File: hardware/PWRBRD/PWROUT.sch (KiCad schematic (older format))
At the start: 0 parts

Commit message: Should now ACTUALLY include power distribution schematic.
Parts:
- added C? (x2): 10uF, symbol C
- added C? (x3): 22uF, symbol C
- added C?: 50nF, symbol C
- added D?: D_Schottky, symbol D_Schottky
- added L?: 1uH, symbol INDUCTOR
- added L?: 4.7uF, symbol INDUCTOR
- added L?: 4mH, symbol INDUCTOR
- added Q?: Q_NPN_BCE, symbol Q_NPN_BCE
- added R?: 10k, symbol R
- added R?: 100m, symbol R
- added R?: 51K, symbol R
- added R?: 2K4, symbol R
- added R?: 1K, symbol R
- added U?: SC189, symbol SC189
- added U?: TS30012, symbol TS30012
- added U?: ZXSC420, symbol ZXSC420
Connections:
- new net: L?.1, U?.5 (LX)
- new net: C?.2, U?.10 (BST)
- new net: R?.2, U?.9 (EN)
- new net: D?.2 (A), L?.2, Q?.2 (C)
- new net: R?.1, R?.2
- new net 16V: C?.1, C?.1, D?.1 (K), R?.1
- new net 3V3: C?.1, L?.2, U?.4 (VOUT)
- new net 5V: C?.1, L?.1, U?.1 (VIN), U?.3 (EN)
- new net DRIVE: Q?.1 (B), U?.4 (DRIVE)
- new net GND: C?.2, C?.2, C?.2, C?.2, C?.2, R?.2, R?.2, U?.14 (PGND), U?.15 (PGND), U?.16 (PGND), U?.2 (GND), U?.2 (STDN), U?.3 (GND), U?.4 (GND)
- new net SENSE: Q?.3 (E), R?.1, U?.5 (SENSE)
- new net VCC: C?.1, L?.1, R?.1, U?.1 (Vcc), U?.11 (VCC), U?.2 (VCC), U?.3 (VCC)
- new net VFB: R?.1, R?.2, U?.6 (VFB)
- new net VSW: C?.1, L?.2, U?.1 (VSW), U?.12 (VSW), U?.13 (VSW), U?.5 (FB)
- no-connect marks 0 -> 3

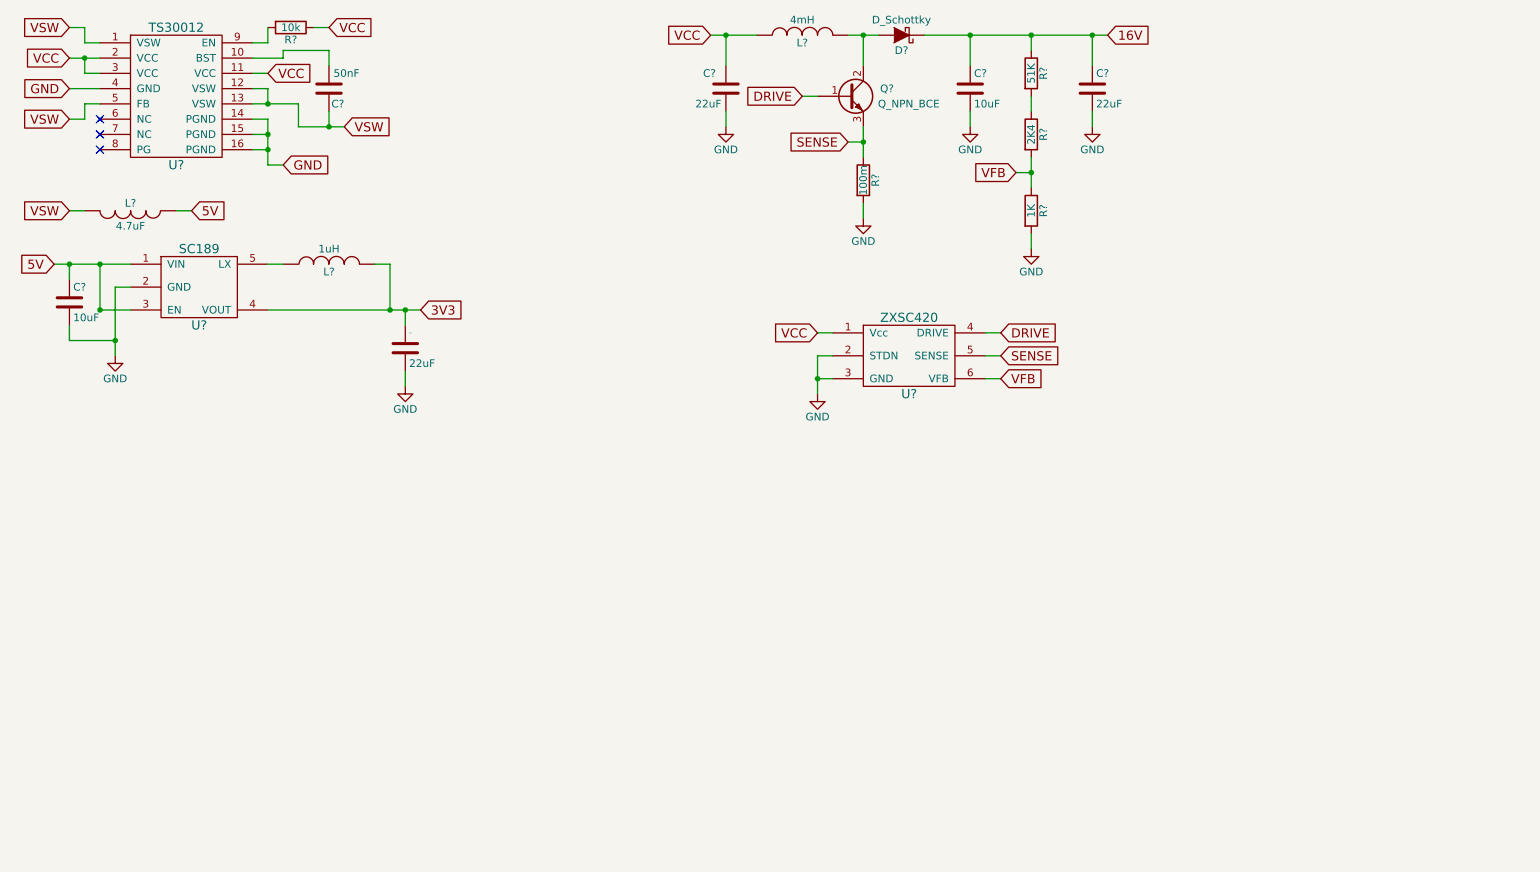
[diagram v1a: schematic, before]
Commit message: Updated the Layout for the BMS portion.
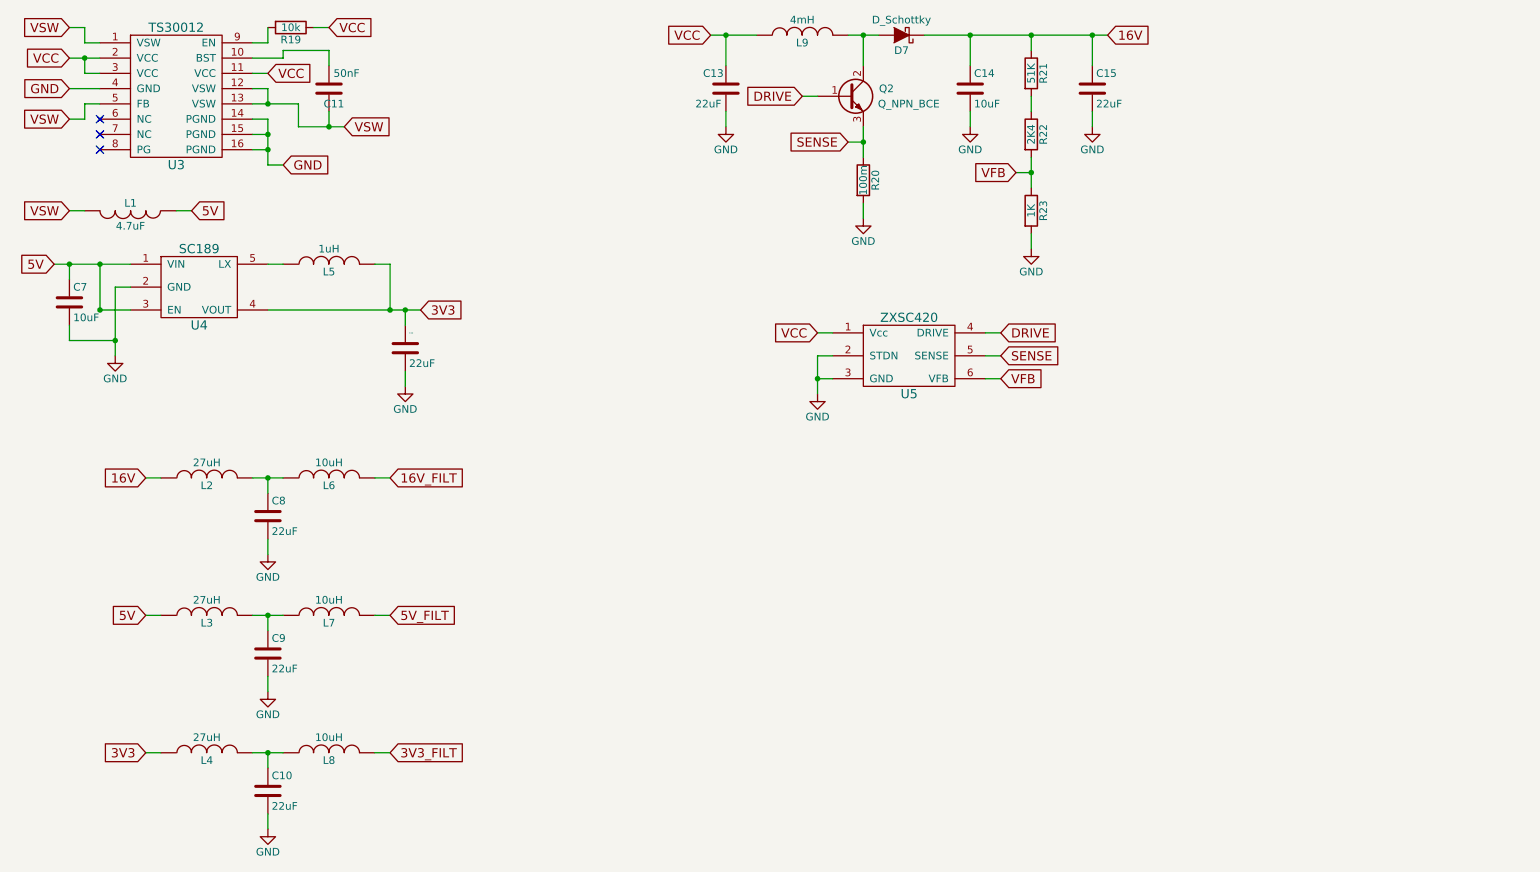
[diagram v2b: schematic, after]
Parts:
- added C10, C8, C9: 22uF, Capacitors_SMD:CP_Elec_5x5.3, symbol C
- added L2, L3, L4: 27uH, Resistors_SMD:R_0805, symbol INDUCTOR
- added L6, L7, L8: 10uH, Resistors_SMD:R_0805, symbol INDUCTOR
- C11, C14, C7: renamed from C?; footprint (none) -> Capacitors_SMD:C_0603
- C12, C13, C15: renamed from C?; footprint (none) -> Capacitors_SMD:CP_Elec_5x5.3
- D7: renamed from D?; footprint (none) -> Resistors_SMD:R_0603
- L1, L5: renamed from L?; footprint (none) -> Resistors_SMD:R_0805
- L9: renamed from L?; footprint (none) -> Choke_Axial_ThroughHole:Choke_Horizontal_RM10mm
- Q2: renamed from Q?; footprint (none) -> TO_SOT_Packages_SMD:SOT-23
- R19, R20, R21, R22, R23: renamed from R?; footprint (none) -> Resistors_SMD:R_0603
- U3: renamed from U?; footprint (none) -> Housings_DFN_QFN:QFN-16-1EP_3x3mm_Pitch0.5mm
- U4: renamed from U?; footprint (none) -> TO_SOT_Packages_SMD:SOT-23-5
- U5: renamed from U?; footprint (none) -> TO_SOT_Packages_SMD:SOT-23-6
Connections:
- net 16V: now also L2.1
- net 3V3: now also L4.1
- net 5V: now also L3.1
- net GND: now also C10.2, C8.2, C9.2
- new net: C8.1, L2.2, L6.1
- new net: C9.1, L3.2, L7.1
- new net: C10.1, L4.2, L8.1
- new net 16V_FILT: L6.2
- new net 3V3_FILT: L8.2
- new net 5V_FILT: L7.2

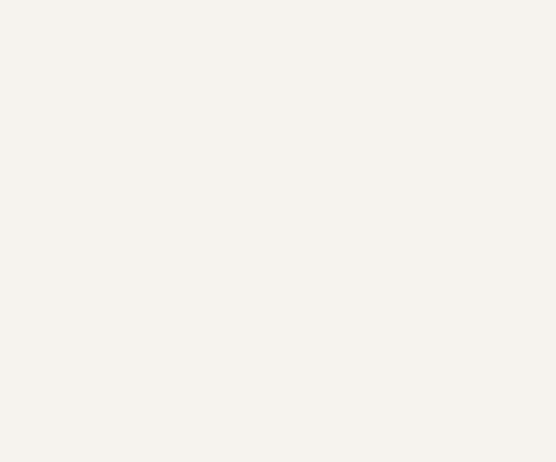
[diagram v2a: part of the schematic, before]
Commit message: Finished laying out and prettifying the BMS/Distribution Board.
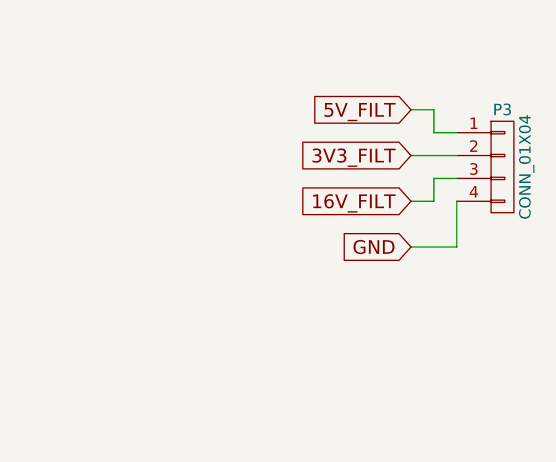
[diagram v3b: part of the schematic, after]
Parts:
- added P3: CONN_01X04, Pin_Headers:Pin_Header_Straight_1x04, symbol CONN_01X04
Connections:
- net 16V_FILT: now also P3.3 (P3)
- net 3V3_FILT: now also P3.2 (P2)
- net 5V_FILT: now also P3.1 (P1)
- net GND: now also P3.4 (P4)
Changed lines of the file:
@@
 LIBS:valves
 LIBS:PWR
+LIBS:PWRBRD-cache
 EELAYER 25 0
 EELAYER END
@@
 Text GLabel 3150 5450 2    60   Input ~ 0
 3V3_FILT
+Wire Wire Line
+	10250 1100 10150 1100
+Wire Wire Line
+	10150 1100 10150 1000
+Wire Wire Line
+	10150 1000 10050 1000
+Wire Wire Line
+	10250 1200 10050 1200
+Wire Wire Line
+	10250 1300 10150 1300
+Wire Wire Line
+	10150 1300 10150 1400
+Wire Wire Line
+	10150 1400 10050 1400
+Text GLabel 10050 1000 0    60   Input ~ 0
+5V_FILT
+Text GLabel 10050 1200 0    60   Input ~ 0
+3V3_FILT
+Text GLabel 10050 1400 0    60   Input ~ 0
+16V_FILT
+$Comp
+L CONN_01X04 P3
+U 1 1 58B0BFC1
+P 10450 1250
+F 0 "P3" H 10450 1500 50  0000 C CNN
+F 1 "CONN_01X04" V 10550 1250 50  0000 C CNN
+F 2 "Pin_Headers:Pin_Header_Straight_1x04" H 10450 1250 50  0001 C CNN
+F 3 "" H 10450 1250 50  0000 C CNN
+	1    10450 1250
+	1    0    0    -1
+$EndComp
+Wire Wire Line
+	10250 1400 10250 1600
+Wire Wire Line
+	10250 1600 10050 1600
+Text GLabel 10050 1600 0    60   Input ~ 0
+GND
 $EndSCHEMATC

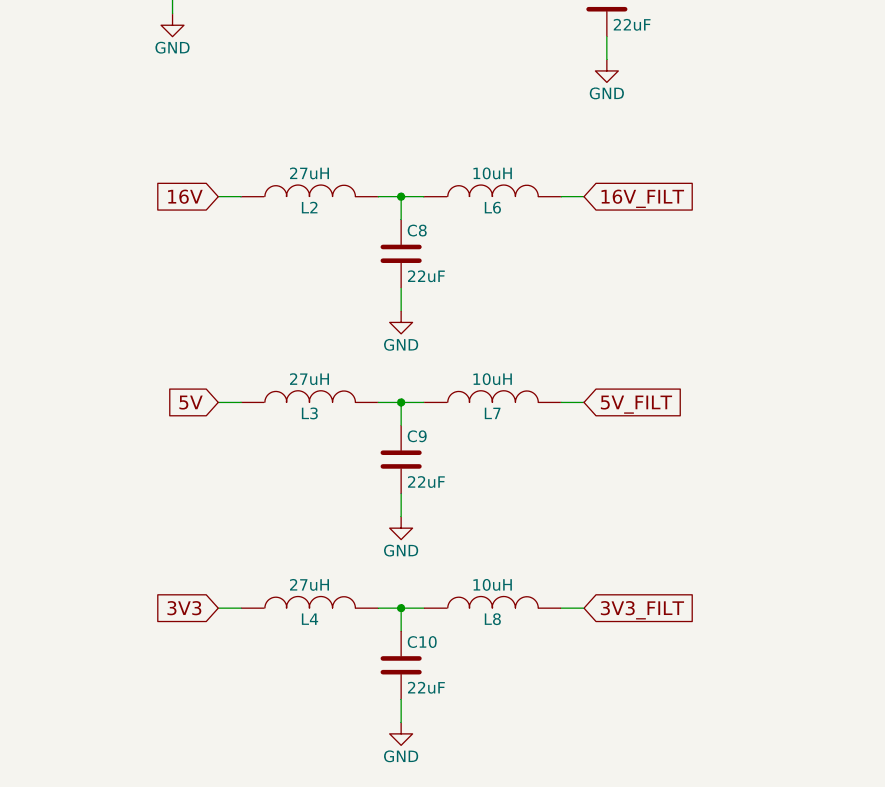
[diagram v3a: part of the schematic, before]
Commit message: Removed some excessive Inductances.
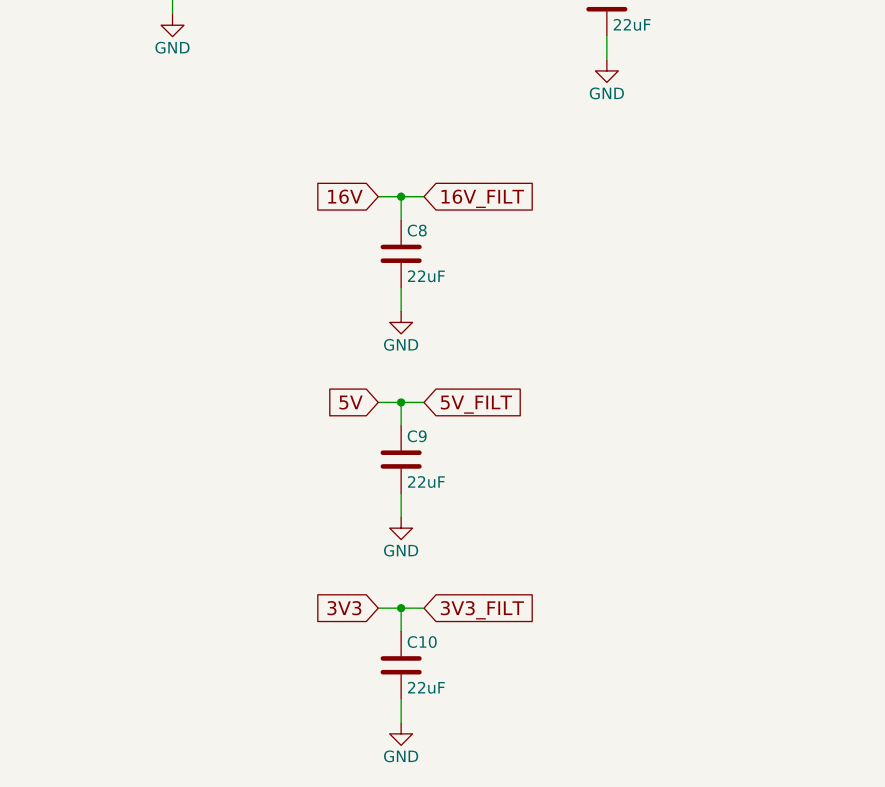
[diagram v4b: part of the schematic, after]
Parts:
- removed L2, L3, L4: 27uH, Resistors_SMD:R_0805, symbol INDUCTOR
- removed L6, L7, L8: 10uH, Resistors_SMD:R_0805, symbol INDUCTOR
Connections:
- net 16V_FILT is gone; now on net 16V: P3.3 (P3)
- net 3V3_FILT is gone; now on net 3V3: P3.2 (P2)
- net 5V_FILT is gone; now on net 5V: P3.1 (P1)
- net 16V: now also C8.1
- net 3V3: now also C10.1
- net 5V: now also C9.1
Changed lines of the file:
@@
 SENSE
-$Comp
-L INDUCTOR L2
-U 1 1 58ADE464
-P 1950 3650
-F 0 "L2" V 1900 3650 50  0000 C CNN
-F 1 "27uH" V 2050 3650 50  0000 C CNN
-F 2 "Resistors_SMD:R_0805" H 1950 3650 50  0001 C CNN
-F 3 "" H 1950 3650 50  0000 C CNN
-	1    1950 3650
-	0    -1   -1   0
-$EndComp
 $Comp
 L C C8
@@
 	1    0    0    -1
 $EndComp
-$Comp
-L INDUCTOR L6
-U 1 1 58ADE610
-P 2750 3650
-F 0 "L6" V 2700 3650 50  0000 C CNN
-F 1 "10uH" V 2850 3650 50  0000 C CNN
-F 2 "Resistors_SMD:R_0805" H 2750 3650 50  0001 C CNN
-F 3 "" H 2750 3650 50  0000 C CNN
-	1    2750 3650
-	0    -1   -1   0
-$EndComp
-Wire Wire Line
-	2250 3650 2450 3650
 Wire Wire Line
 	2350 3750 2350 3650
 Connection ~ 2350 3650
 Wire Wire Line
-	1650 3650 1550 3650
-Wire Wire Line
-	3050 3650 3150 3650
+	2250 3650 2450 3650
 Wire Wire Line
 	2350 4050 2350 4150
@@
 	1    0    0    -1
 $EndComp
-Text GLabel 1550 3650 0    60   Input ~ 0
+Text GLabel 2250 3650 0    60   Input ~ 0
 16V
-Text GLabel 3150 3650 2    60   Input ~ 0
+Text GLabel 2450 3650 2    60   Input ~ 0
 16V_FILT
-$Comp
-L INDUCTOR L3
-U 1 1 58ADEA7D
-P 1950 4550
-F 0 "L3" V 1900 4550 50  0000 C CNN
-F 1 "27uH" V 2050 4550 50  0000 C CNN
-F 2 "Resistors_SMD:R_0805" H 1950 4550 50  0001 C CNN
-F 3 "" H 1950 4550 50  0000 C CNN
-	1    1950 4550
-	0    -1   -1   0
-$EndComp
 $Comp
 L C C9
@@
 	1    0    0    -1
 $EndComp
-$Comp
-L INDUCTOR L7
-U 1 1 58ADEA89
-P 2750 4550
-F 0 "L7" V 2700 4550 50  0000 C CNN
-F 1 "10uH" V 2850 4550 50  0000 C CNN
-F 2 "Resistors_SMD:R_0805" H 2750 4550 50  0001 C CNN
-F 3 "" H 2750 4550 50  0000 C CNN
-	1    2750 4550
-	0    -1   -1   0
-$EndComp
-Wire Wire Line
-	2250 4550 2450 4550
 Wire Wire Line
 	2350 4650 2350 4550
 Connection ~ 2350 4550
 Wire Wire Line
-	1650 4550 1550 4550
-Wire Wire Line
-	3050 4550 3150 4550
+	2250 4550 2450 4550
 Wire Wire Line
 	2350 4950 2350 5050
@@
 	1    0    0    -1
 $EndComp
-Text GLabel 1550 4550 0    60   Input ~ 0
+Text GLabel 2250 4550 0    60   Input ~ 0
 5V
-Text GLabel 3150 4550 2    60   Input ~ 0
+Text GLabel 2450 4550 2    60   Input ~ 0
 5V_FILT
-$Comp
-L INDUCTOR L4
-U 1 1 58ADEC3C
-P 1950 5450
-F 0 "L4" V 1900 5450 50  0000 C CNN
-F 1 "27uH" V 2050 5450 50  0000 C CNN
-F 2 "Resistors_SMD:R_0805" H 1950 5450 50  0001 C CNN
-F 3 "" H 1950 5450 50  0000 C CNN
-	1    1950 5450
-	0    -1   -1   0
-$EndComp
 $Comp
 L C C10
@@
 	1    0    0    -1
 $EndComp
-$Comp
-L INDUCTOR L8
-U 1 1 58ADEC48
-P 2750 5450
-F 0 "L8" V 2700 5450 50  0000 C CNN
-F 1 "10uH" V 2850 5450 50  0000 C CNN
-F 2 "Resistors_SMD:R_0805" H 2750 5450 50  0001 C CNN
-F 3 "" H 2750 5450 50  0000 C CNN
-	1    2750 5450
-	0    -1   -1   0
-$EndComp
-Wire Wire Line
-	2250 5450 2450 5450
 Wire Wire Line
 	2350 5550 2350 5450
 Connection ~ 2350 5450
 Wire Wire Line
-	1650 5450 1550 5450
-Wire Wire Line
-	3050 5450 3150 5450
+	2250 5450 2450 5450
 Wire Wire Line
 	2350 5850 2350 5950
@@
 	1    0    0    -1
 $EndComp
-Text GLabel 1550 5450 0    60   Input ~ 0
+Text GLabel 2250 5450 0    60   Input ~ 0
 3V3
-Text GLabel 3150 5450 2    60   Input ~ 0
+Text GLabel 2450 5450 2    60   Input ~ 0
 3V3_FILT
 Wire Wire Line
